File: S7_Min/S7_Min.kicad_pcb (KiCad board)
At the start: 4 copper layers, 89 x 72 mm, 171 parts, among them J1 Barrel_Jack_Switch, J2 XILINX_JTAG, J3 HDMI_A, J4 Conn_02x15_Odd_Even, Q1 DMN2020L, Q2 DMN63D8LDW, Q3 DMN63D8LDW, Q4 DMN63D8LDW, Q5 DMN2020L, U1 TPS65581, U2 XC7S50-FTGB196, U3 REF3012, U4 QSPI_Flash_SOIC8, U5 MT47H128M16XX, U6 AZ1117-5.0, U7 TPD12S521, X1 DSC61XX

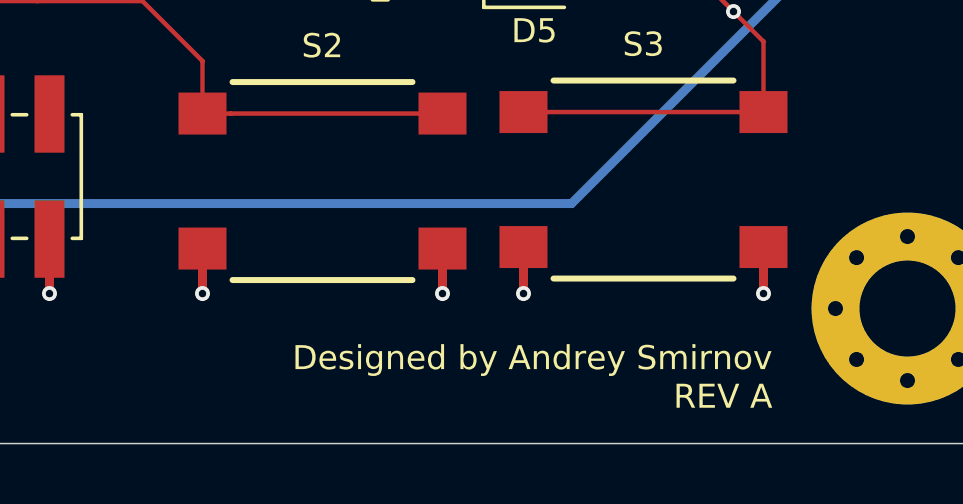
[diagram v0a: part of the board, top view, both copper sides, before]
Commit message: added silkscreen labels to buttons "CFG_RESET" and "SYS_RESET"
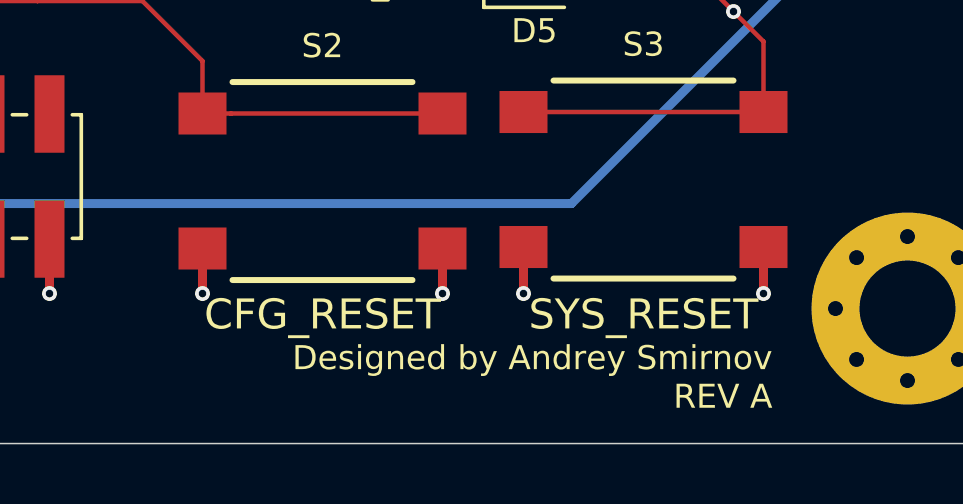
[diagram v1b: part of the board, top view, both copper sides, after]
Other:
- board text added: "CFG_RESET"
- board text added: "SYS_RESET"
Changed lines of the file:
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@@
   (general
     (thickness 1.6)
-    (drawings 44)
+    (drawings 46)
     (tracks 3510)
     (zones 0)
@@
   (layers
     (0 F.Cu signal)
-    (1 In1.Cu power)
-    (2 In2.Cu power)
-    (31 B.Cu signal)
+    (1 In1.Cu power hide)
+    (2 In2.Cu power hide)
+    (31 B.Cu signal hide)
     (32 B.Adhes user)
     (33 F.Adhes user)
@@
     )
   )
+  (gr_text SYS_RESET (at 166.7 119.7) (layer F.SilkS)
+    (effects (font (size 1 1) (thickness 0.15)))
+  )
+  (gr_text CFG_RESET (at 156 119.7) (layer F.SilkS)
+    (effects (font (size 1 1) (thickness 0.15)))
+  )
   (gr_text "Designed by Andrey Smirnov\nREV A" (at 171 121.793) (layer F.SilkS)

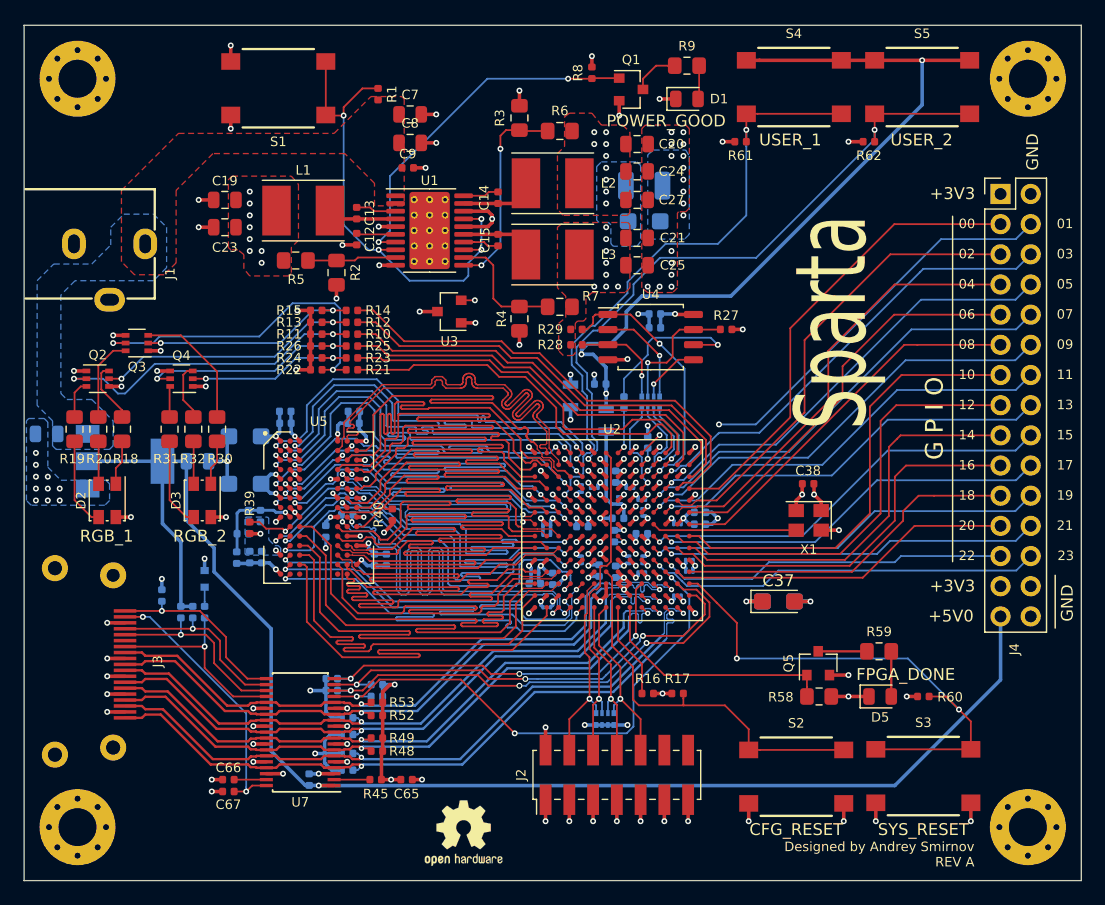
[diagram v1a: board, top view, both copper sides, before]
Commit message: fixed the layout after adding missing PAD pin to TPS65581 symbol :facepalm: added some exposed ground on the bottom side to improve thermals.
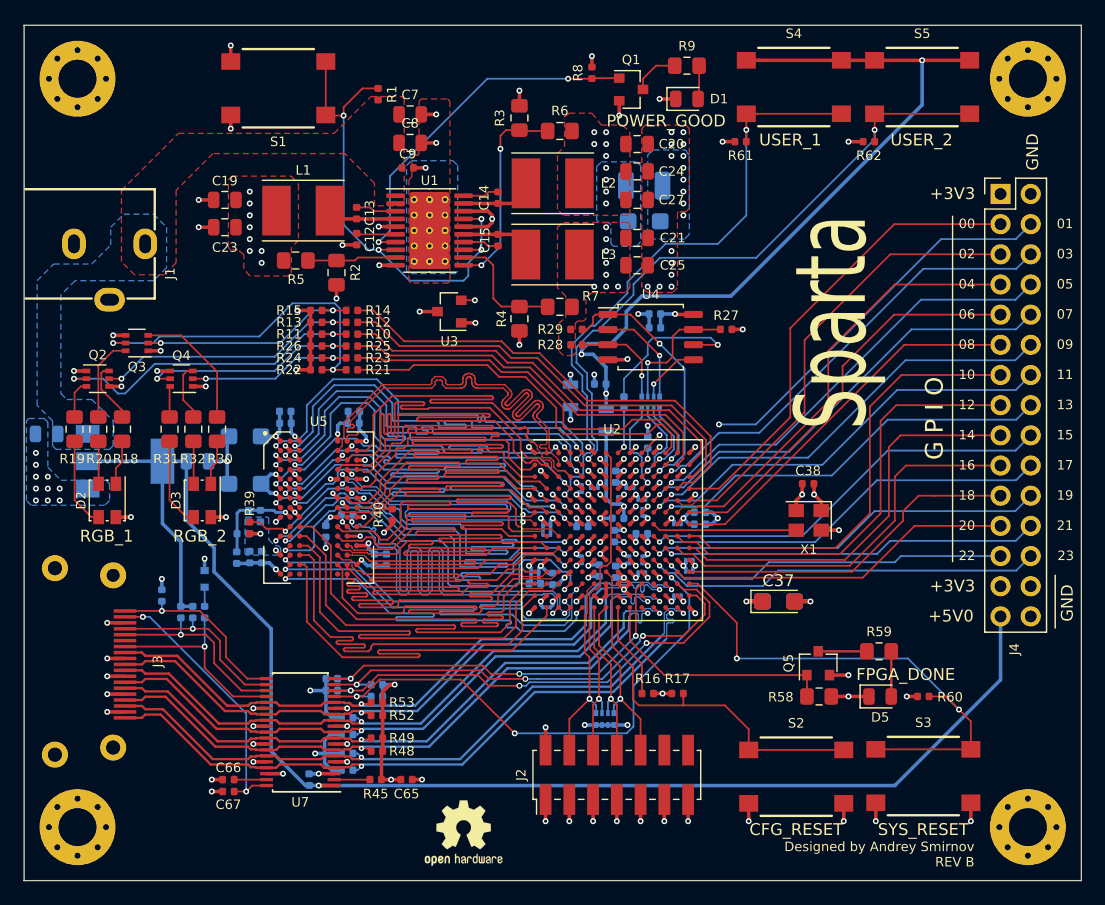
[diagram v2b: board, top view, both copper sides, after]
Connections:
- U1 pad 21: (no net) -> GND
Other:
- board text added: "Designed by Andrey Smirnov REV B"
- board text removed: "Designed by Andrey Smirnov REV A"
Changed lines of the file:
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@@
   (layers
     (0 F.Cu signal)
-    (1 In1.Cu power hide)
-    (2 In2.Cu power hide)
-    (31 B.Cu signal hide)
+    (1 In1.Cu power)
+    (2 In2.Cu power)
+    (31 B.Cu signal)
     (32 B.Adhes user)
     (33 F.Adhes user)
@@
     (trace_clearance 0.1)
     (zone_clearance 0.15)
-    (zone_45_only no)
+    (zone_45_only yes)
     (trace_min 0.1)
     (via_size 0.5)
@@
     (mod_text_size 0.8 0.8)
     (mod_text_width 0.12)
-    (pad_size 1.524 1.524)
-    (pad_drill 0.762)
+    (pad_size 2.6 2)
+    (pad_drill 1.6)
     (pad_to_mask_clearance 0.051)
     (solder_mask_min_width 0.1)
@@
       (net 1 GND))
     (pad 1 thru_hole oval (at 0 3 90) (size 2.6 2) (drill oval 1.6 1) (layers *.Cu *.Mask)
-      (net 20 +12V))
+      (net 20 +12V) (zone_connect 2))
     (model ../../kicad-3dmodels/models/CUI_PJ-102B.step
       (offset (xyz 0 10.7 6.7))
@@
     (pad "" smd roundrect (at -0.69 0.86) (size 1.11 1.38) (layers F.Paste) (roundrect_rratio 0.225225))
     (pad "" smd roundrect (at -0.69 -0.86) (size 1.11 1.38) (layers F.Paste) (roundrect_rratio 0.225225))
-    (pad 21 smd roundrect (at 0 0) (size 3.2 5.8) (layers B.Cu) (roundrect_rratio 0.078125))
-    (pad 21 thru_hole circle (at 1.3 2.6) (size 0.6 0.6) (drill 0.3) (layers *.Cu))
-    (pad 21 thru_hole circle (at 0 2.6) (size 0.6 0.6) (drill 0.3) (layers *.Cu))
-    (pad 21 thru_hole circle (at -1.3 2.6) (size 0.6 0.6) (drill 0.3) (layers *.Cu))
-    (pad 21 thru_hole circle (at 1.3 1.3) (size 0.6 0.6) (drill 0.3) (layers *.Cu))
-    (pad 21 thru_hole circle (at 0 1.3) (size 0.6 0.6) (drill 0.3) (layers *.Cu))
-    (pad 21 thru_hole circle (at -1.3 1.3) (size 0.6 0.6) (drill 0.3) (layers *.Cu))
-    (pad 21 thru_hole circle (at 1.3 0) (size 0.6 0.6) (drill 0.3) (layers *.Cu))
-    (pad 21 thru_hole circle (at 0 0) (size 0.6 0.6) (drill 0.3) (layers *.Cu))
-    (pad 21 thru_hole circle (at -1.3 0) (size 0.6 0.6) (drill 0.3) (layers *.Cu))
-    (pad 21 thru_hole circle (at 1.3 -1.3) (size 0.6 0.6) (drill 0.3) (layers *.Cu))
-    (pad 21 thru_hole circle (at 0 -1.3) (size 0.6 0.6) (drill 0.3) (layers *.Cu))
-    (pad 21 thru_hole circle (at -1.3 -1.3) (size 0.6 0.6) (drill 0.3) (layers *.Cu))
-    (pad 21 thru_hole circle (at 1.3 -2.6) (size 0.6 0.6) (drill 0.3) (layers *.Cu))
-    (pad 21 thru_hole circle (at 0 -2.6) (size 0.6 0.6) (drill 0.3) (layers *.Cu))
-    (pad 21 thru_hole circle (at -1.3 -2.6) (size 0.6 0.6) (drill 0.3) (layers *.Cu))
-    (pad 21 smd roundrect (at 0 0) (size 3.4 6.5) (layers F.Cu) (roundrect_rratio 0.073529))
+    (pad 21 smd roundrect (at 0 0) (size 3.2 5.8) (layers B.Cu) (roundrect_rratio 0.078125)
+      (net 1 GND))
+    (pad 21 thru_hole circle (at 1.3 2.6) (size 0.6 0.6) (drill 0.3) (layers *.Cu)
+      (net 1 GND))
+    (pad 21 thru_hole circle (at 0 2.6) (size 0.6 0.6) (drill 0.3) (layers *.Cu)
+      (net 1 GND))
+    (pad 21 thru_hole circle (at -1.3 2.6) (size 0.6 0.6) (drill 0.3) (layers *.Cu)
+      (net 1 GND))
+    (pad 21 thru_hole circle (at 1.3 1.3) (size 0.6 0.6) (drill 0.3) (layers *.Cu)
+      (net 1 GND))
+    (pad 21 thru_hole circle (at 0 1.3) (size 0.6 0.6) (drill 0.3) (layers *.Cu)
+      (net 1 GND))
+    (pad 21 thru_hole circle (at -1.3 1.3) (size 0.6 0.6) (drill 0.3) (layers *.Cu)
+      (net 1 GND))
+    (pad 21 thru_hole circle (at 1.3 0) (size 0.6 0.6) (drill 0.3) (layers *.Cu)
+      (net 1 GND))
+    (pad 21 thru_hole circle (at 0 0) (size 0.6 0.6) (drill 0.3) (layers *.Cu)
+      (net 1 GND))
+    (pad 21 thru_hole circle (at -1.3 0) (size 0.6 0.6) (drill 0.3) (layers *.Cu)
+      (net 1 GND))
+    (pad 21 thru_hole circle (at 1.3 -1.3) (size 0.6 0.6) (drill 0.3) (layers *.Cu)
+      (net 1 GND))
+    (pad 21 thru_hole circle (at 0 -1.3) (size 0.6 0.6) (drill 0.3) (layers *.Cu)
+      (net 1 GND))
+    (pad 21 thru_hole circle (at -1.3 -1.3) (size 0.6 0.6) (drill 0.3) (layers *.Cu)
+      (net 1 GND))
+    (pad 21 thru_hole circle (at 1.3 -2.6) (size 0.6 0.6) (drill 0.3) (layers *.Cu)
+      (net 1 GND))
+    (pad 21 thru_hole circle (at 0 -2.6) (size 0.6 0.6) (drill 0.3) (layers *.Cu)
+      (net 1 GND))
+    (pad 21 thru_hole circle (at -1.3 -2.6) (size 0.6 0.6) (drill 0.3) (layers *.Cu)
+      (net 1 GND))
+    (pad 21 smd roundrect (at 0 0) (size 3.4 6.5) (layers F.Cu) (roundrect_rratio 0.07400000000000001)
+      (net 1 GND) (zone_connect 2))
     (pad "" smd roundrect (at 0 0) (size 2.75 3.43) (layers F.Mask) (roundrect_rratio 0.090909))
     (model ${KISYS3DMOD}/Package_SO.3dshapes/HTSSOP-20-1EP_4.4x6.5mm_P0.65mm_EP3.4x6.5mm_Mask2.75x3.43mm.wrl
@@
     (effects (font (size 1 1) (thickness 0.15)))
   )
-  (gr_text "Designed by Andrey Smirnov\nREV A" (at 171 121.793) (layer F.SilkS)
+  (gr_text "Designed by Andrey Smirnov\nREV B" (at 171 121.793) (layer F.SilkS)
     (effects (font (size 0.8 0.8) (thickness 0.12)) (justify right))
   )
@@
   )
   (zone (net 1) (net_name GND) (layer In1.Cu) (hatch edge 0.508)
-    (connect_pads (clearance 0.15))
+    (connect_pads yes (clearance 0.15))
     (min_thickness 0.2)
     (fill yes (arc_segments 32) (thermal_gap 0.3) (thermal_bridge_width 0.508))
@@
   (zone (net 3) (net_name +1V0) (layer In2.Cu) (hatch edge 0.508)
     (priority 1)
-    (connect_pads (clearance 0.15))
+    (connect_pads yes (clearance 0.15))
     (min_thickness 0.2)
     (fill yes (arc_segments 32) (thermal_gap 0.3) (thermal_bridge_width 0.508))
@@
   (zone (net 2) (net_name +1V8) (layer In2.Cu) (hatch edge 0.508)
     (priority 1)
-    (connect_pads (clearance 0.15))
+    (connect_pads yes (clearance 0.15))
     (min_thickness 0.15)
     (fill yes (arc_segments 32) (thermal_gap 0.3) (thermal_bridge_width 0.508))
@@
   )
   (zone (net 8) (net_name +3V3) (layer In2.Cu) (hatch edge 0.508)
-    (connect_pads (clearance 0.15))
+    (connect_pads yes (clearance 0.15))
     (min_thickness 0.15)
     (fill yes (arc_segments 32) (thermal_gap 0.3) (thermal_bridge_width 0.508))
@@
       )
     )
+  )
+  (zone (net 1) (net_name GND) (layer F.Cu) (hatch edge 0.508)
+    (priority 1)
+    (connect_pads (clearance 0.15))
+    (min_thickness 0.2)
+    (fill yes (arc_segments 32) (thermal_gap 0.3) (thermal_bridge_width 0.508))
+    (polygon
+      (pts
+        (xy 126.85 58.4) (xy 126.85 73.55) (xy 126.7 73.7) (xy 123.55 73.7) (xy 123.4 73.55)
+        (xy 123.4 65) (xy 123.65 64.75) (xy 123.65 63.2) (xy 123.9 62.95) (xy 124.1 62.95)
+        (xy 124.25 62.8) (xy 124.25 58.4) (xy 124.45 58.2) (xy 126.65 58.2)
+      )
+    )
+  )
+  (zone (net 1) (net_name GND) (layer B.Cu) (hatch edge 0.508)
+    (priority 1)
+    (connect_pads yes (clearance 0.15))
+    (min_thickness 0.2)
+    (fill yes (arc_segments 32) (thermal_gap 0.3) (thermal_bridge_width 0.508))
+    (polygon
+      (pts
+        (xy 127.5 63.8) (xy 127.5 72.7) (xy 127.3 72.9) (xy 123.4 72.9) (xy 123.2 72.7)
+        (xy 123.2 63.8) (xy 123.6 63.4) (xy 127.1 63.4)
+      )
+    )
+  )
+  (zone (net 0) (net_name "") (layer B.Mask) (hatch edge 0.508)
+    (priority 1)
+    (connect_pads (clearance 0.15))
+    (min_thickness 0.2)
+    (fill yes (arc_segments 32) (thermal_gap 0.3) (thermal_bridge_width 0.508))
+    (polygon
+      (pts
+        (xy 127.3 64) (xy 127.2 72.4) (xy 127 72.6) (xy 123.6 72.6) (xy 123.4 72.4)
+        (xy 123.4 64) (xy 123.8 63.6) (xy 126.9 63.6)
+      )
+    )

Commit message: REV C: - fixed power disable button connections (:facepalm:) - "FPGA_DONE" and "POWER_GOOD" LEDs were connected backwards
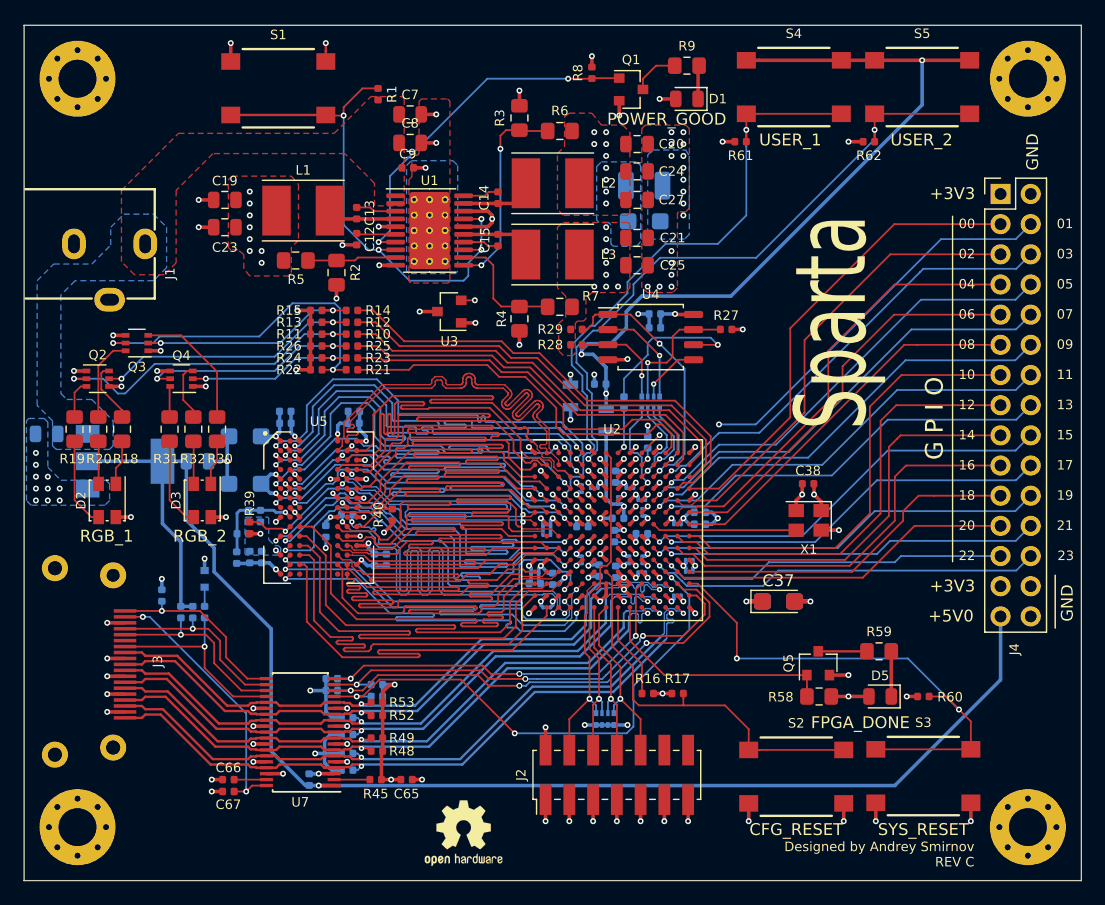
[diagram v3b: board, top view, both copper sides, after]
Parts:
- C45, C47, C48, C49, C50, C64, C65, C66, C67: value 0.1uF -> 0.1 uF
- C46: value 10nF -> 10 nF
- C51, C53, C55, C57: value 1.0uF -> 1 uF
- turned D1 to 180 degrees
- turned D5 to 180 degrees
- turned S1 to 180 degrees
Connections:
- D1 pad 1: +3V3 -> Net-(D1-Pad1)
- D1 pad 2: Net-(D1-Pad2) -> +3V3
- D5 pad 1: +3V3 -> Net-(D5-Pad1)
- D5 pad 2: Net-(D5-Pad2) -> +3V3
- R59 pad 2: Net-(D5-Pad2) -> Net-(D5-Pad1)
- R9 pad 2: Net-(D1-Pad2) -> Net-(D1-Pad1)
- S1 pad 1: Net-(R1-Pad1) -> GND
- S1 pad 3: GND -> Net-(R1-Pad1)
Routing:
- net Net-(D5-Pad2): track 3.80 -> 0.00 mm
- net Net-(D5-Pad1): track 0.00 -> 3.80 mm
- net Net-(R1-Pad1): track 41.8 -> 45.3 mm
- net Net-(D1-Pad1): track 0.00 -> 2.96 mm
- net Net-(D1-Pad2): track 2.84 -> 0.00 mm
- net GND: track 181.0 -> 181.6 mm
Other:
- board text added: "Designed by Andrey Smirnov REV C"
- board text removed: "Designed by Andrey Smirnov REV B"

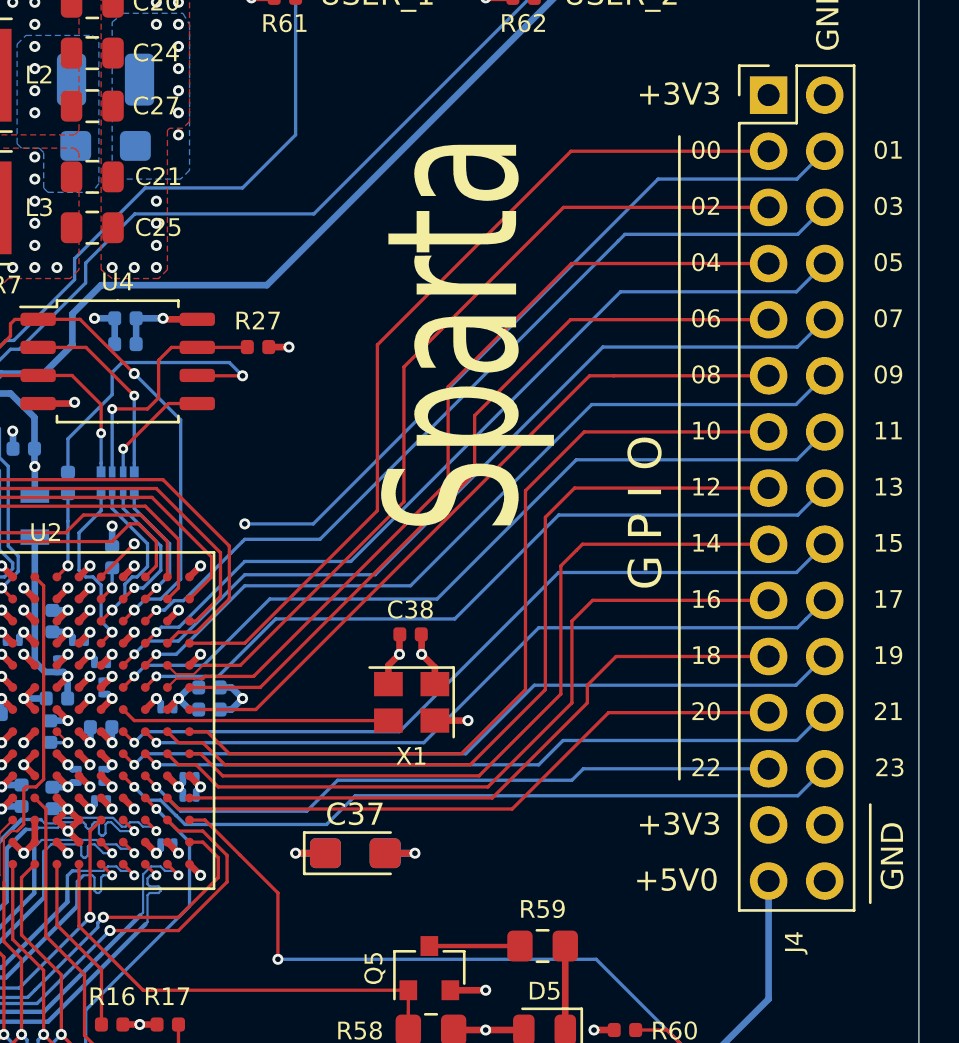
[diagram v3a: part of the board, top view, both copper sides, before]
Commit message: matched length of all GPIO traces to 40.7±0.1 mm
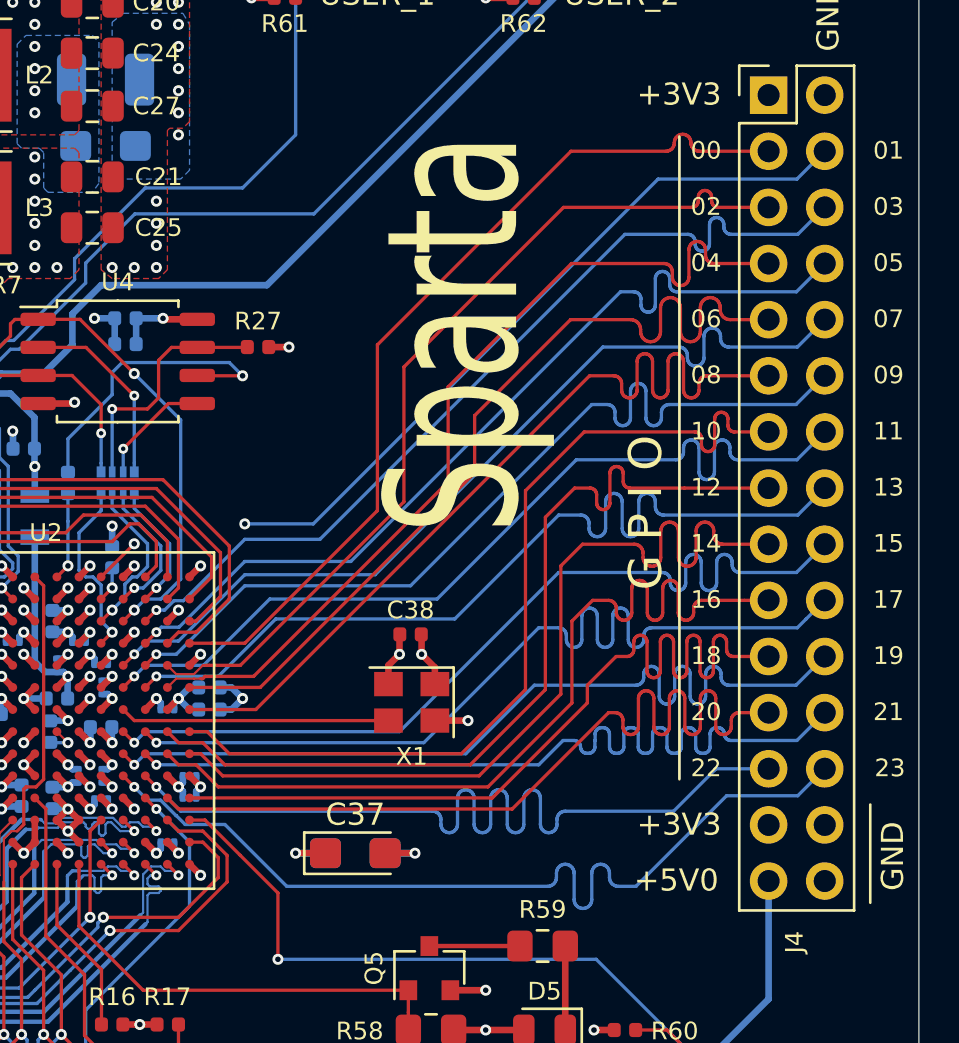
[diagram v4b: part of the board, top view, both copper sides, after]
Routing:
- net GPIO_20: track 29.2 -> 40.7 mm
- net GPIO_18: track 29.3 -> 40.7 mm
- net GPIO_22: track 29.7 -> 40.7 mm
- net GPIO_21: track 31.9 -> 40.8 mm
- net GPIO_8: track 32.5 -> 40.6 mm
- net GPIO_16: track 33.5 -> 40.7 mm
- net GPIO_17: track 33.6 -> 40.7 mm
- net GPIO_23: track 33.7 -> 40.6 mm
- net GPIO_19: track 34.0 -> 40.7 mm
- net GPIO_14: track 34.4 -> 40.6 mm
- net GPIO_13: track 34.5 -> 40.7 mm
- net GPIO_6: track 34.6 -> 40.7 mm
- net GPIO_15: track 35.7 -> 40.7 mm
- net GPIO_9: track 36.2 -> 40.7 mm
- net GPIO_11: track 36.5 -> 40.7 mm
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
